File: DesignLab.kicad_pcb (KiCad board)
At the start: 2 copper layers, 45 parts, among them J1 Conn_01x06_Male, J2 USB_B_Micro, J3 Conn_01x03_Male, J4 Conn_01x12, J5 Conn_01x02_Male, Q1 IRLML2060, Q2 IRLML6402, Q3 BC817, SW1 SW_Push, SW2 SW_Push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

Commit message: v0.4 - MM - updated schematic
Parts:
- removed C11: 10uF, Capacitor_SMD:C_1206_3216Metric_Pad1.33x1.80mm_HandSolder
- removed C12: 100nF, Capacitor_SMD:C_0603_1608Metric_Pad1.08x0.95mm_HandSolder
- removed NTC1: R, Connector_Wire:SolderWire-0.5sqmm_1x02_P4.6mm_D0.9mm_OD2.1mm
- removed R15: 10k, Resistor_SMD:R_0603_1608Metric_Pad0.98x0.95mm_HandSolder
- added U5: TP4054-42, Package_TO_SOT_SMD:SOT-23-5_HandSoldering, F.Cu at (197.2, 38.1)
- C8: footprint Capacitor_SMD:C_0805_2012Metric_Pad1.18x1.45mm_HandSolder -> Capacitor_SMD:C_1206_3216Metric_Pad1.33x1.80mm_HandSolder
- C9: value 10uF -> 100nF; footprint Capacitor_SMD:C_1206_3216Metric_Pad1.33x1.80mm_HandSolder -> Capacitor_SMD:C_0603_1608Metric_Pad1.08x0.95mm_HandSolder
- J2: footprint Connector_USB:USB_Micro-B_Amphenol_10104110_Horizontal -> Connector_USB:USB_Micro-B_Amphenol_10118194_Horizontal
- R11: value R -> 1k
- R12: value R -> 10k
- R13: value 2,4k -> 1k
- R2: value 100k -> 100R
- R4: value 100R -> 10k
- R5: value 10k -> 100k
- U2: value MIC5353-3.3YMT -> AP2127N-3.3; footprint Package_DFN_QFN:MLF-6-1EP_1.6x1.6mm_P0.5mm_EP0.5x1.26mm -> Package_TO_SOT_SMD:SOT-23
- U3: value 74AUC2G34 -> 74LVC1G125; footprint Package_TO_SOT_SMD:SOT-23-6_Handsoldering -> Package_TO_SOT_SMD:SOT-23-5_HandSoldering
- U4: value TP4056 -> 74LVC1G125; footprint Package_SO:HSOP-8-1EP_3.9x4.9mm_P1.27mm_EP2.41x3.1mm -> Package_TO_SOT_SMD:SOT-23-5_HandSoldering
- Y1: footprint Crystal:Crystal_SMD_Abracon_ABS25-4Pin_8.0x3.8mm -> Crystal:Crystal_SMD_3215-2Pin_3.2x1.5mm
- moved C9 73.1 mm to (199.9, 60.6), turned to 90 degrees
- moved Q2 69.3 mm to (201.9, 38.1)
- moved SW1 65.6 mm to (204.2, 57.4), turned to -90 degrees
- moved C8 63.9 mm to (196.1, 60.7)
- moved R5 61.1 mm to (202.8, 53.1), turned to 180 degrees
- moved SW2 56.9 mm to (204.2, 49.5), turned to -90 degrees
- moved U1 55.0 mm to (189.2, 41.4)
- moved D2 52.5 mm to (196.8, 41.9)
- moved C3 51.8 mm to (200.9, 45.7)
- moved J1 51.6 mm to (177.8, 38.4)
- moved J2 50.3 mm to (180.1, 56.4)
- moved Y1 45.4 mm to (186.9, 56.1)
- moved R12 44.6 mm to (201.9, 62.5), turned to 90 degrees
- moved R9 44.6 mm to (191.3, 58.7)
- moved R13 44.0 mm to (199.4, 49.3), turned to -90 degrees
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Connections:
- C10 pad 1: /SW_1 -> /SW_2
- C7 pad 1: Net-(C7-Pad1) -> VCC
- C8 pad 1: VCC -> +5V
- C9 pad 1: +5V -> /SW_1
- R11 pad 1: +5V -> Net-(R11-Pad1)
- R11 pad 2: Net-(NTC1-Pad2) -> GND
- R12 pad 1: Net-(NTC1-Pad2) -> VCC
- R12 pad 2: GND -> /SW_1
- R13 pad 1: Net-(R13-Pad1) -> /BAT_CH
- R13 pad 2: GND -> VCC
- R14 pad 2: /SW_1 -> /SW_2
- R2 pad 1: +BATT -> Net-(J3-Pad1)
- R2 pad 2: Net-(Q1-Pad3) -> Net-(D2-Pad3)
- R3 pad 1: Net-(J3-Pad1) -> Net-(J3-Pad3)
- R3 pad 2: Net-(D2-Pad3) -> Net-(D1-Pad3)
- R4 pad 1: Net-(J3-Pad3) -> GND
- R5 pad 1: GND -> +BATT
- R5 pad 2: Net-(D1-Pad3) -> Net-(Q1-Pad3)
- U2 pad 1: +BATT -> GND
- U2 pad 2: GND -> VCC
- U3 pad 1: Net-(D2-Pad3) -> GND
- U3 pad 2: GND -> /UART.TX
- U3 pad 3: /UART.TX -> GND
- U4 pad 1: Net-(NTC1-Pad2) -> GND
- U4 pad 2: Net-(R13-Pad1) -> Net-(D2-Pad3)
- U4 pad 4: +5V -> /UART.RX
- U4 pad 5: +BATT -> VCC

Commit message: Update DesignLab.kicad_pcb
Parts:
- added ?: , , F.Cu at (216.9, 46.3)
- added ?: , , F.Cu at (191.9, 83.3)
- added ?: , , F.Cu at (216.9, 83.3)
- added REF**: MountingHole_3.2mm_M3, MountingHole:MountingHole_3.2mm_M3, F.Cu at (191.9, 46.3)
- moved SW1 60.5 mm to (146.5, 75.7), turned to 0 degrees
- moved D2 40.8 mm to (201.8, 82.4), turned to 90 degrees
- moved SW2 40.7 mm to (173.1, 75.7), turned to 0 degrees
- moved D1 40.4 mm to (197.5, 82.4), turned to 90 degrees
- moved U4 38.3 mm to (205.9, 82.3), turned to 90 degrees
- moved Y1 35.9 mm to (211.3, 82.5), turned to 90 degrees
- moved J3 34.0 mm to (191.3, 71.0)
- moved R13 31.1 mm to (216.8, 75.0), turned to 0 degrees
- moved R14 30.3 mm to (216.8, 77.4)
- moved Q3 29.9 mm to (216.8, 51.5)
- moved U3 28.4 mm to (203.1, 75.3), turned to 90 degrees
- moved J5 28.3 mm to (209.8, 46.0), turned to 90 degrees
- moved J2 27.0 mm to (160.7, 75.1)
- moved U5 26.4 mm to (216.3, 56.3)
- moved R9 26.1 mm to (216.7, 64.5)
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
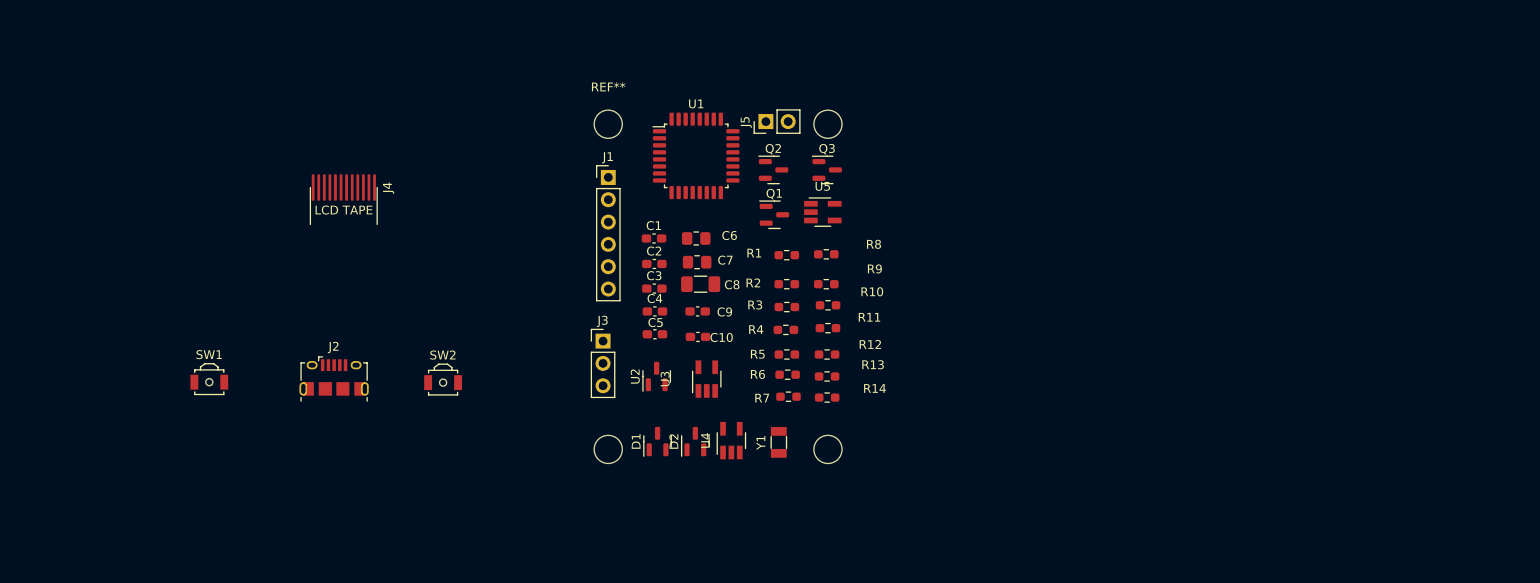
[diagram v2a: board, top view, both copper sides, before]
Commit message: zmiany 9.12 15:00
brak c11-c13 w schemacie pcb, próby autoroutingu
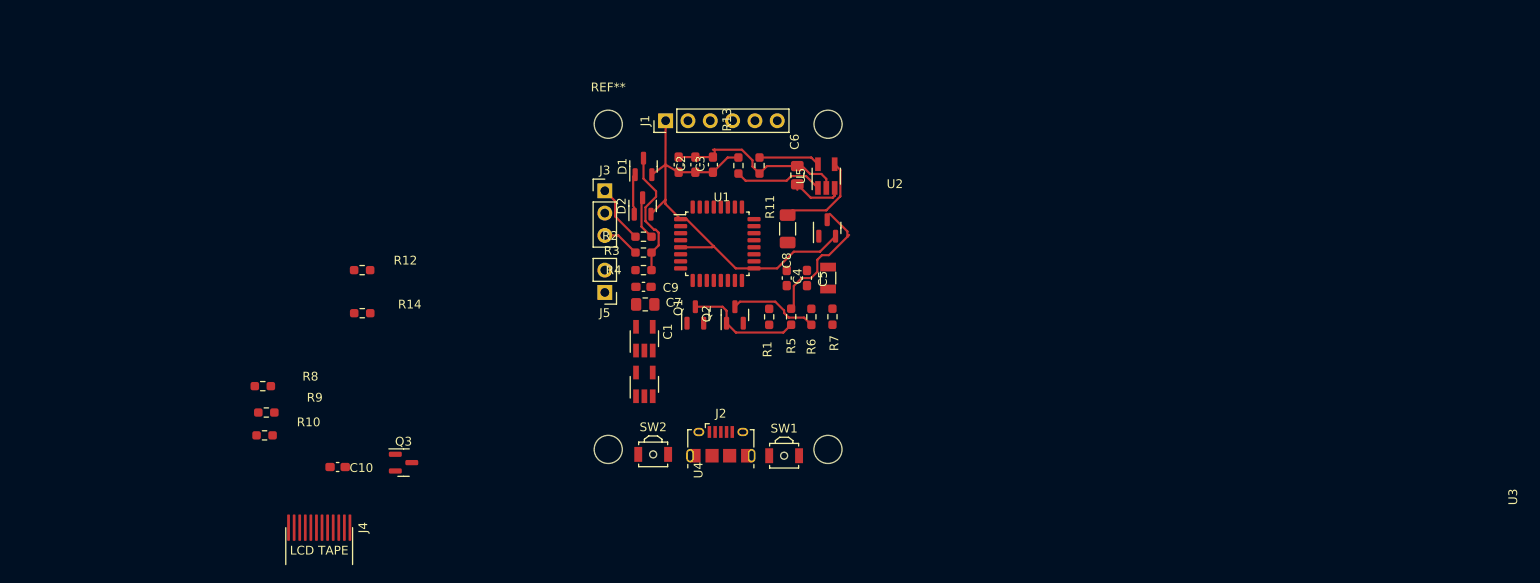
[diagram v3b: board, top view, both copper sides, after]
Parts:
- moved SW1 65.9 mm to (211.9, 84.0)
- moved R8 65.8 mm to (152.6, 76.1)
- moved R10 65.8 mm to (152.8, 81.7)
- moved R9 65.4 mm to (153.0, 79.1)
- moved Q3 58.6 mm to (168.6, 84.8)
- moved R12 53.8 mm to (163.9, 62.9)
- moved R14 53.8 mm to (163.9, 67.8)
- moved J2 44.7 mm to (204.7, 82.7)
- moved C10 43.6 mm to (161.1, 85.3)
- moved J4 38.8 mm to (159.0, 92.2)
- moved D1 31.3 mm to (195.9, 51.1)
- moved D2 27.5 mm to (195.8, 55.6)
- moved J5 26.7 mm to (191.5, 65.4), turned to 180 degrees
- moved R13 26.0 mm to (206.7, 51.0), turned to 90 degrees
- moved U2 25.7 mm to (216.8, 58.1)
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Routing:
- net VCC: track 0.00 -> 50.6 mm
- net GND: track 0.00 -> 25.1 mm
- net +BATT: track 0.00 -> 22.2 mm
- net Net-(D1-Pad3): track 0.00 -> 14.9 mm
- net Net-(Q1-Pad3): track 0.00 -> 13.3 mm
- net +5V: track 0.00 -> 10.8 mm
- net Net-(Q2-Pad3): track 0.00 -> 10.5 mm
- net /BAT_CH: track 0.00 -> 10.2 mm
- net Net-(R11-Pad1): track 0.00 -> 6.97 mm
- net Net-(J3-Pad1): track 0.00 -> 6.67 mm
- net Net-(D2-Pad3): track 0.00 -> 4.96 mm
- net Net-(J3-Pad3): track 0.00 -> 4.29 mm

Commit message: edit
edit
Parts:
- J2, J4, SW1, SW2: moved to B.Cu
- moved J4 45.5 mm to (204.4, 90.1)
- moved R10 9.39 mm to (160.1, 75.8)
- moved R12 9.39 mm to (171.2, 57.0)
- moved C10 9.39 mm to (168.4, 79.4)
- moved Q3 9.39 mm to (175.9, 78.9)
- moved R14 9.39 mm to (171.2, 61.9)
- moved R8 9.39 mm to (159.9, 70.2)
- moved R9 9.39 mm to (160.3, 73.2)
- turned J2 to 180 degrees
- turned SW1 to 180 degrees
- turned SW2 to 180 degrees
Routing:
- net VCC: track 50.6 -> 0.68 mm
- net GND: track 25.1 -> 1.55 mm
- net +BATT: track 22.2 -> 1.11 mm
- net Net-(D1-Pad3): track 14.9 -> 0.00 mm
- net Net-(Q1-Pad3): track 13.3 -> 0.00 mm
- net Net-(Q2-Pad3): track 10.5 -> 0.32 mm
- net /BAT_CH: track 10.2 -> 0.00 mm
- net +5V: track 10.8 -> 0.76 mm
- net Net-(R11-Pad1): track 6.97 -> 0.00 mm
- net Net-(J3-Pad1): track 6.67 -> 0.00 mm
- net Net-(D2-Pad3): track 4.96 -> 0.18 mm
- net Net-(J3-Pad3): track 4.29 -> 0.00 mm

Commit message: Update DesignLab.kicad_pcb
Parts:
- moved R8 12.2 mm to (169.4, 62.5)
- moved R9 12.2 mm to (169.8, 65.5)
- moved R10 12.2 mm to (169.6, 68.1)
- moved R12 8.89 mm to (178.6, 61.9)
- moved R14 8.36 mm to (178.6, 65.8)
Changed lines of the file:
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@@
   )
   (footprint "Resistor_SMD:R_0603_1608Metric_Pad0.98x0.95mm_HandSolder" (layer "F.Cu")
-    (at 171.2 61.9)
+    (at 178.6 65.8)
     (descr "Resistor SMD 0603 (1608 Metric), square (rectangular) end terminal, IPC_7351 nominal with elongated pad for handsoldering. (Body size source: IPC-SM-782 page 72, https://www.pcb-3d.com/wordpress/wp-content/uploads/ipc-sm-782a_amendment_1_and_2.pdf), generated with kicad-footprint-generator")
     (tags "resistor handsolder")
@@
   )
   (footprint "Resistor_SMD:R_0603_1608Metric_Pad0.98x0.95mm_HandSolder" (layer "F.Cu")
-    (at 171.1875 57 180)
+    (at 178.6 61.9 180)
     (descr "Resistor SMD 0603 (1608 Metric), square (rectangular) end terminal, IPC_7351 nominal with elongated pad for handsoldering. (Body size source: IPC-SM-782 page 72, https://www.pcb-3d.com/wordpress/wp-content/uploads/ipc-sm-782a_amendment_1_and_2.pdf), generated with kicad-footprint-generator")
     (tags "resistor handsolder")
@@
   )
   (footprint "Resistor_SMD:R_0603_1608Metric_Pad0.98x0.95mm_HandSolder" (layer "F.Cu")
-    (at 160.2875 73.2)
+    (at 169.8 65.5)
     (descr "Resistor SMD 0603 (1608 Metric), square (rectangular) end terminal, IPC_7351 nominal with elongated pad for handsoldering. (Body size source: IPC-SM-782 page 72, https://www.pcb-3d.com/wordpress/wp-content/uploads/ipc-sm-782a_amendment_1_and_2.pdf), generated with kicad-footprint-generator")
     (tags "resistor handsolder")
@@
   )
   (footprint "Resistor_SMD:R_0603_1608Metric_Pad0.98x0.95mm_HandSolder" (layer "F.Cu")
-    (at 160.0875 75.8)
+    (at 169.6 68.1)
     (descr "Resistor SMD 0603 (1608 Metric), square (rectangular) end terminal, IPC_7351 nominal with elongated pad for handsoldering. (Body size source: IPC-SM-782 page 72, https://www.pcb-3d.com/wordpress/wp-content/uploads/ipc-sm-782a_amendment_1_and_2.pdf), generated with kicad-footprint-generator")
     (tags "resistor handsolder")
@@
   )
   (footprint "Resistor_SMD:R_0603_1608Metric_Pad0.98x0.95mm_HandSolder" (layer "F.Cu")
-    (at 159.8875 70.2 180)
+    (at 169.4 62.5 180)
     (descr "Resistor SMD 0603 (1608 Metric), square (rectangular) end terminal, IPC_7351 nominal with elongated pad for handsoldering. (Body size source: IPC-SM-782 page 72, https://www.pcb-3d.com/wordpress/wp-content/uploads/ipc-sm-782a_amendment_1_and_2.pdf), generated with kicad-footprint-generator")
     (tags "resistor handsolder")

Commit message: v0.8 updated layout
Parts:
- removed ? (x3): , 
- removed REF**: MountingHole_3.2mm_M3, MountingHole:MountingHole_3.2mm_M3
- added C10: 100n, Capacitor_SMD:C_0805_2012Metric_Pad1.18x1.45mm_HandSolder, F.Cu at (169.9, 40.4)
- added C7: 100n, Capacitor_SMD:C_0805_2012Metric_Pad1.18x1.45mm_HandSolder, F.Cu at (164.8, 46.7)
- added C9: 100n, Capacitor_SMD:C_0805_2012Metric_Pad1.18x1.45mm_HandSolder, F.Cu at (164.8, 43.7)
- added H1: MountingHole, MountingHole:MountingHole_2.2mm_M2_ISO7380, F.Cu at (217.3, 83.7)
- added H2: MountingHole, MountingHole:MountingHole_2.2mm_M2_ISO7380, F.Cu at (217.3, 44.9)
- added H3: MountingHole, MountingHole:MountingHole_2.2mm_M2_ISO7380, F.Cu at (191.5, 44.9)
- added H4: MountingHole, MountingHole:MountingHole_2.2mm_M2_ISO7380, F.Cu at (191.5, 83.7)
- added Y1: Crystal, Crystal:Crystal_SMD_3215-2Pin_3.2x1.5mm, F.Cu at (165.0, 40.5)
- C12: renamed from C9; value 100nF -> 100n; footprint Capacitor_SMD:C_0603_1608Metric_Pad1.08x0.95mm_HandSolder -> Capacitor_SMD:C_0805_2012Metric_Pad1.18x1.45mm_HandSolder
- C13: renamed from C10; value 100nF -> 100n; footprint Capacitor_SMD:C_0603_1608Metric_Pad1.08x0.95mm_HandSolder -> Capacitor_SMD:C_0805_2012Metric_Pad1.18x1.45mm_HandSolder
- J1: footprint Connector_PinHeader_2.54mm:PinHeader_1x06_P2.54mm_Vertical -> Connector_PinHeader_2.54mm:PinHeader_2x03_P2.54mm_Vertical
- SW1, SW2: footprint Button_Switch_SMD:SW_SPST_B3U-3000P-B -> Button_Switch_SMD:SW_SPST_TSS02-035NT
- moved J4 21.5 mm to (201.6, 68.8)
- moved J5 18.6 mm to (195.4, 47.3)
- moved J3 12.0 mm to (199.2, 44.7), turned to 90 degrees
- moved J1 9.74 mm to (208.1, 47.3)
- moved R12 1.39 mm to (179.3, 63.1)
- moved SW2 0.60 mm to (196.6, 84.3), turned to 0 degrees
- moved J2 0.43 mm to (204.4, 83.0)
- moved SW1 0.41 mm to (212.2, 84.3), turned to 0 degrees
- renumbered C8 to C11, C7 to C8
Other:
- board outline added: 30 x 43 mm
- board text added: "<"
- board text added: "B+ B-"
- board text added: "PROG"
- board text added: "RX"
- board text added: "TX"

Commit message: v0.9 updated schematic
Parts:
- removed the Y1 at (216.9, 63.8)
- moved Y1 57.1 mm to (217.2, 63.5), turned to 90 degrees
- moved C3 0.55 mm to (204.3, 51.0)
- moved C12 0.15 mm to (196.0, 64.7)
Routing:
- net GND: track 1.55 -> 0.17 mm

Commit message: layout PCB draw 0.1version
prawie skończone
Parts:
- added TP1: TestPoint, TestPoint:TestPoint_Pad_1.5x1.5mm, F.Cu at (208.1, 54.2)
- added TP2: TestPoint, TestPoint:TestPoint_Pad_1.5x1.5mm, F.Cu at (204.4, 53.7)
- added TP3: TestPoint, TestPoint:TestPoint_Pad_1.5x1.5mm, F.Cu at (201.8, 49.4)
- added TP4: TestPoint, TestPoint:TestPoint_Pad_1.5x1.5mm, F.Cu at (204.4, 51.1)
- added TP5: TestPoint, TestPoint:TestPoint_Pad_1.5x1.5mm, F.Cu at (199.4, 65.7)
- added TP6: TestPoint, TestPoint:TestPoint_Pad_1.5x1.5mm, F.Cu at (218.2, 68.5)
- added TP7: TestPoint, TestPoint:TestPoint_Pad_1.5x1.5mm, F.Cu at (218.2, 70.6)
- added TP8: TestPoint, TestPoint:TestPoint_Pad_1.5x1.5mm, F.Cu at (218.2, 72.6)
- added TP9: TestPoint, TestPoint:TestPoint_Pad_1.5x1.5mm, F.Cu at (199.1, 48.0)
- moved C9 55.1 mm to (214.6, 67.4)
- moved C7 54.9 mm to (214.6, 69.9)
- moved C10 43.7 mm to (202.9, 69.1), turned to 180 degrees
- moved R10 40.1 mm to (209.0, 75.4), turned to 180 degrees
- moved R8 40.0 mm to (208.8, 69.7)
- moved R9 39.0 mm to (208.8, 67.5), turned to 180 degrees
- moved R12 36.5 mm to (212.2, 78.9), turned to 0 degrees
- moved C6 34.8 mm to (192.0, 79.5), turned to 0 degrees
- moved Q3 33.8 mm to (209.1, 72.7)
- moved U5 31.4 mm to (192.7, 72.5), turned to 0 degrees
- moved U2 30.8 mm to (192.0, 76.4), turned to 180 degrees
- moved C13 28.4 mm to (196.7, 81.5), turned to 180 degrees
- moved R11 25.1 mm to (196.2, 72.5)
- moved C12 23.3 mm to (212.3, 81.4)
- moved R14 23.1 mm to (197.9, 78.5), turned to -90 degrees
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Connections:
- C10 pad 2: GND -> VCC
- U1 pad 18: unconnected-(U1-Pad18) -> /PA8
- U1 pad 21: unconnected-(U1-Pad21) -> /PA11
- U1 pad 22: unconnected-(U1-Pad22) -> /PA12
- U1 pad 27: unconnected-(U1-Pad27) -> /PB4
- U1 pad 28: unconnected-(U1-Pad28) -> /PB5
- U1 pad 29: unconnected-(U1-Pad29) -> /PB6
- U1 pad 30: unconnected-(U1-Pad30) -> /PB7
- U1 pad 31: unconnected-(U1-Pad31) -> /BOOTO
- U1 pad 9: unconnected-(U1-Pad9) -> /PA3
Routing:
- net VCC: track 0.68 -> 93.7 mm, vias 0 -> 1
- net /SW_2: track 0.00 -> 44.1 mm, vias 0 -> 2
- net +BATT: track 1.11 -> 45.0 mm
- net /SW_1: track 0.00 -> 38.7 mm, vias 0 -> 2
- net /LCD_RST: track 0.00 -> 25.8 mm, vias 0 -> 1
- net /SWDIO: track 0.00 -> 23.7 mm, vias 0 -> 2
- net /A_BAT_EN: track 0.00 -> 22.8 mm, vias 0 -> 2
- net /NRST: track 0.00 -> 22.0 mm, vias 0 -> 1
- net /SWCLK: track 0.00 -> 21.5 mm, vias 0 -> 2
- net /UART.TX: track 0.00 -> 21.2 mm, vias 0 -> 2
- net +5V: track 0.76 -> 21.5 mm, vias 0 -> 1
- net /PA12: track 0.00 -> 20.7 mm, vias 0 -> 2
- net Net-(J3-Pad1): track 0.00 -> 18.5 mm
- net /PA8: track 0.00 -> 16.1 mm, vias 0 -> 2
- net /LCD_SDA: track 0.00 -> 16.0 mm, vias 0 -> 1
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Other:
- board text added: "AGH-CLK-01"
